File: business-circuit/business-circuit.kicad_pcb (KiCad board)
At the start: 2 copper layers, 11 parts, among them U1 NT3H2111W0FHKH

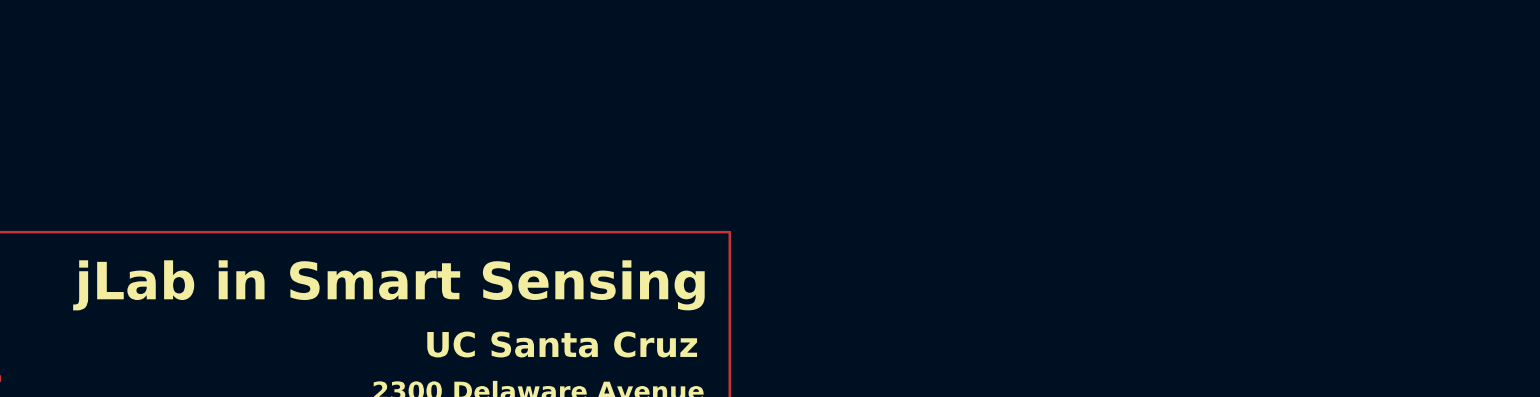
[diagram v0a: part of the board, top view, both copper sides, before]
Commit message: need to add antenna
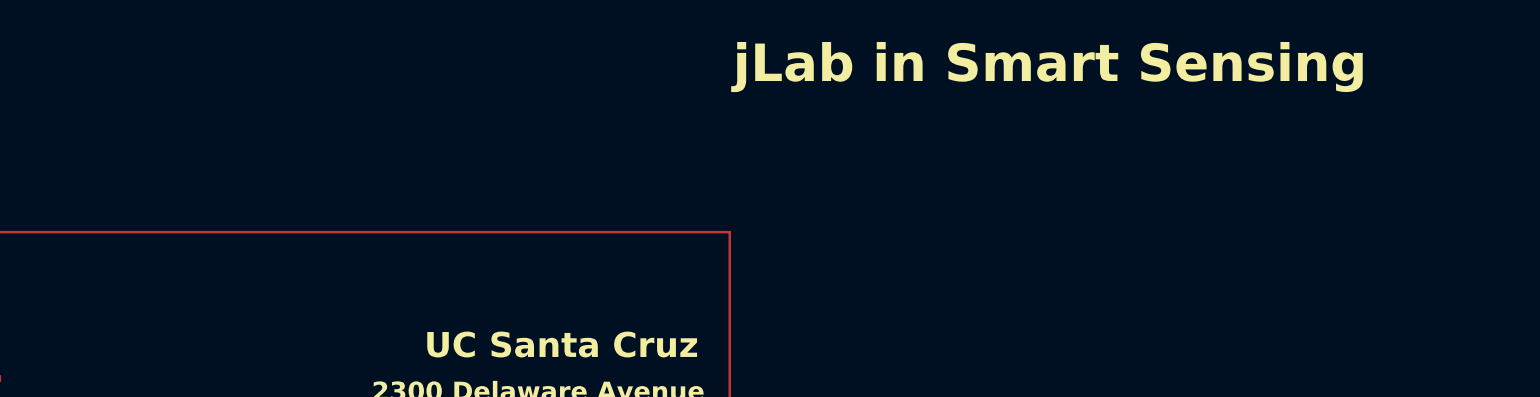
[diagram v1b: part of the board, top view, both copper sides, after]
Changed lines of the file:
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@@
 	)
 	(gr_text "jLab in Smart Sensing"
-		(at 78.5 55.75 0)
+		(at 131.25 38.25 0)
 		(layer "F.SilkS")
 		(effects

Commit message: pre importing antenna
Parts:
- removed TP1: Signal, TestPoint:TestPoint_Pad_1.0x1.0mm
- removed TP2: SDA, TestPoint:TestPoint_Pad_1.0x1.0mm
- removed TP3: SCL, TestPoint:TestPoint_Pad_1.0x1.0mm
- removed TP4: VCC, TestPoint:TestPoint_Pad_1.0x1.0mm
- removed TP5: GND, TestPoint:TestPoint_Pad_1.0x1.0mm
- added C2: 130 pF, Capacitor_SMD:C_0402_1005Metric_Pad0.74x0.62mm_HandSolder, F.Cu at (115.0, 82.1)
- added R4: 220 Ω, Resistor_SMD:R_0402_1005Metric_Pad0.72x0.64mm_HandSolder, F.Cu at (123.6, 74.4)
- C1: value 220nF -> 200 nF; footprint Capacitor_SMD:C_0402_1005Metric -> Capacitor_SMD:C_0402_1005Metric_Pad0.74x0.62mm_HandSolder
- R1, R2, R3: value 10kΩ -> 10 kΩ; footprint Resistor_SMD:R_0402_1005Metric -> Resistor_SMD:R_0402_1005Metric_Pad0.72x0.64mm_HandSolder
- moved R3 72.3 mm to (126.7, 73.8)
- moved R1 69.4 mm to (124.2, 72.2)
- moved U1 63.7 mm to (122.7, 81.9), turned to 0 degrees
- moved R2 61.9 mm to (126.7, 76.2)
- moved C1 54.5 mm to (124.0, 77.5)
- moved D1 51.8 mm to (120.8, 75.0), turned to 0 degrees
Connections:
- net GNDREF renamed GNDR
- C1 pad 1: Net-(D1-A) -> Net-(U1-VCC)
- R1 pad 1: Net-(D1-A) -> Net-(U1-VCC)
- R2 pad 1: Net-(D1-A) -> Net-(U1-VCC)
- R3 pad 1: Net-(D1-A) -> Net-(U1-VCC)
- U1 pad 6: Net-(D1-A) -> Net-(U1-VCC)
- U1 pad 7: Net-(D1-A) -> Net-(U1-VCC)
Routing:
- net Net-(U1-LA): track 5.33 -> 228.0 mm, vias 0 -> 2
- net Net-(D1-A): track 34.8 -> 2.25 mm, vias 1 -> 0
- net Net-(U1-VCC): track 0.00 -> 11.5 mm
- net Net-(U1-SDA): track 11.7 -> 4.12 mm
- net Net-(U1-SCL): track 18.3 -> 13.0 mm
- net GNDR: track 6.95 -> 3.29 mm, vias 0 -> 1
- net Net-(U1-FD): track 14.9 -> 16.5 mm, vias 2 -> 0

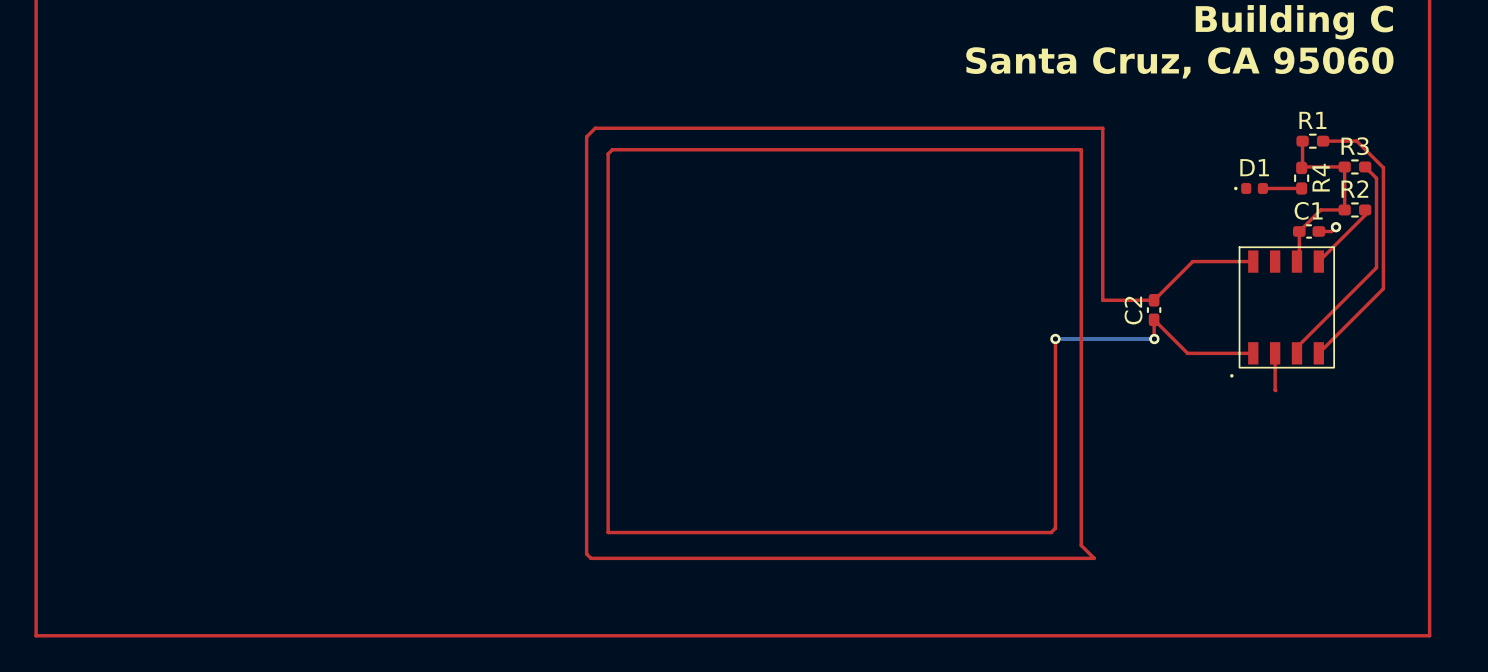
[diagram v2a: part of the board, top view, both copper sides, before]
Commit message: antenna broke SRC :(
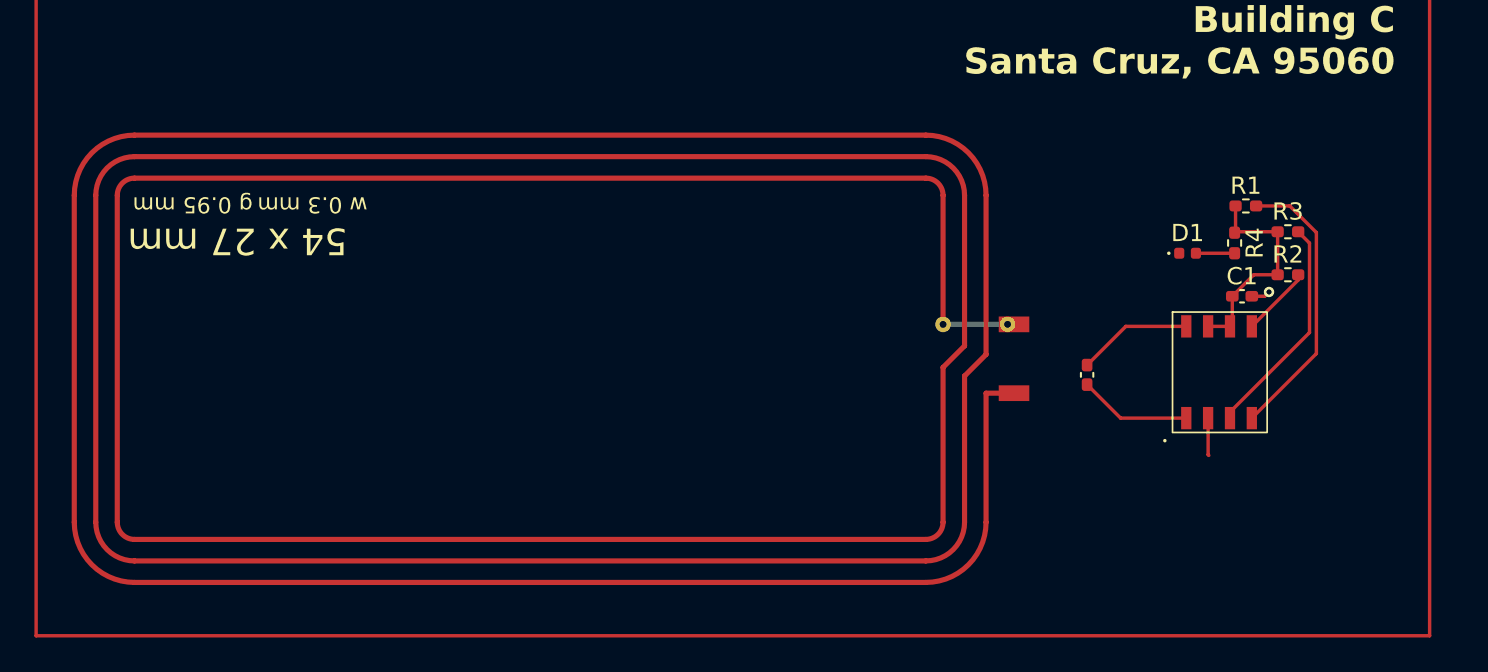
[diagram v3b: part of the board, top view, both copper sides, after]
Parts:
- added AE1: Antenna, Library:54X27_3TURNS_THIN, F.Cu at (80.0, 84.9)
- R1: value 10 kΩ -> 220 Ω
- R4: value 220 Ω -> 10 kΩ
- moved C1 5.42 mm to (120.1, 81.3)
- moved R1 5.42 mm to (120.3, 76.0)
- moved C2 5.42 mm to (111.1, 85.8)
- moved D1 5.42 mm to (116.9, 78.8)
- moved R2 5.42 mm to (122.8, 80.0)
- moved R3 5.42 mm to (122.8, 77.5)
- moved U1 5.42 mm to (118.8, 85.7)
- moved R4 5.42 mm to (119.7, 78.2)
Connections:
- C2 pad 2: Net-(U1-LA) -> Net-(U1-LB)
- R1 pad 2: Net-(U1-FD) -> Net-(D1-A)
- R2 pad 2: Net-(U1-SDA) -> Net-(U1-SCL)
- R3 pad 2: Net-(U1-SCL) -> Net-(U1-SDA)
- R4 pad 2: Net-(D1-A) -> Net-(U1-FD)
- U1 pad 8: Net-(U1-LA) -> Net-(U1-LB)
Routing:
- net Net-(U1-LA): track 228.0 -> 6.57 mm, vias 2 -> 0
- net Net-(U1-LB): track 0.00 -> 6.70 mm
- net Net-(U1-VCC): track 11.5 -> 12.8 mm
